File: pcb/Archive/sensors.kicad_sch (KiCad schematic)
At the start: 4 parts, among them U2 HDC1080, U3 LTR-303ALS-01

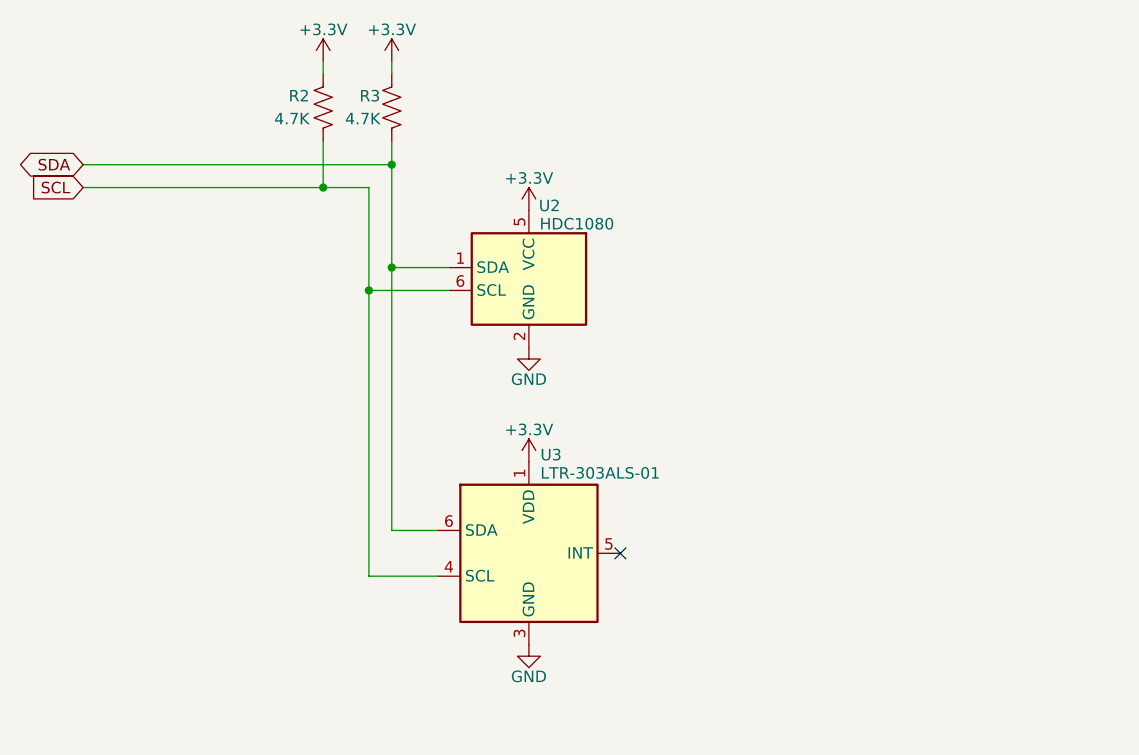
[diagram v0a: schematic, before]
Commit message: Added interfaces and fully routed PCB
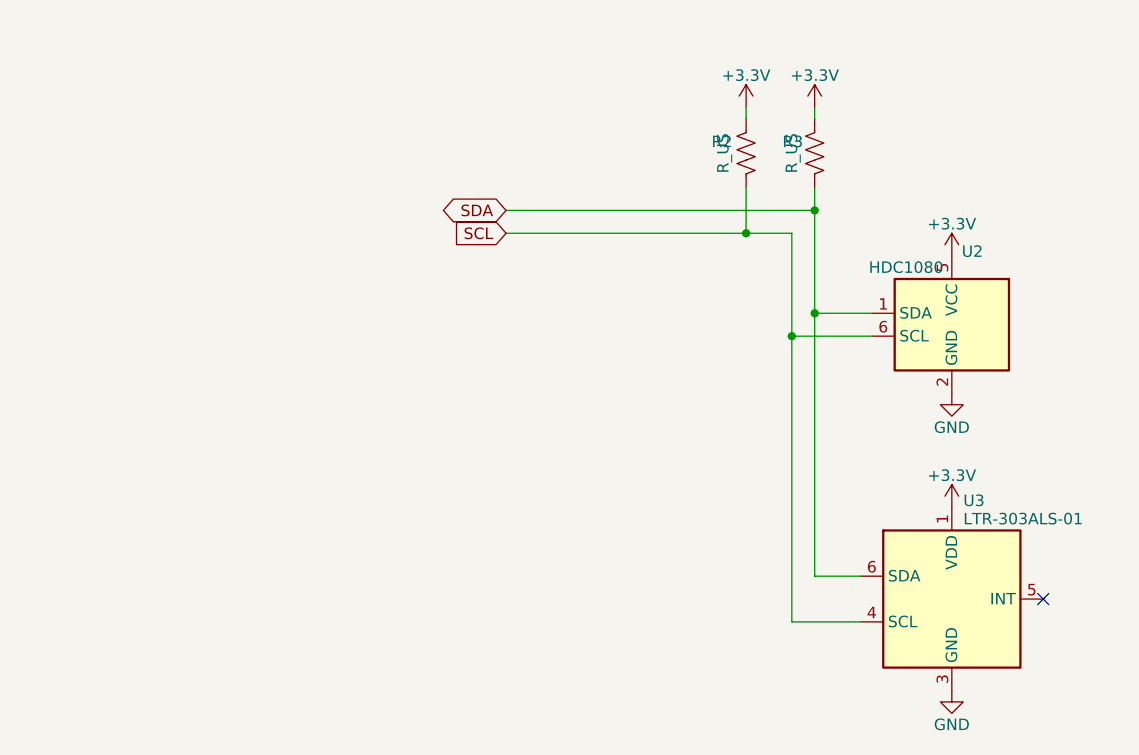
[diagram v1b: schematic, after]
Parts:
- R2, R3: value 4.7K -> R_US; footprint Resistor_SMD:R_0603_1608Metric -> (none); Digikey 541-3993-2-ND -> (none); LCSC C2907166 -> (none); MN FOJAN -> (none); MPN FRC0603J472 TS -> (none); Mouser 71-CRCW06034K70JNEAC -> (none)
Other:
- moved on the sheet: R2, R3, U2, U3
